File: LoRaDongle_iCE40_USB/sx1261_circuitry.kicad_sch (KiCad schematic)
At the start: 41 parts, among them J5 142-0701-801, J8 Jumper, U3 SX1261IMLTRT, U4 SKY13587-378LF, Y2 Crystal_GND24

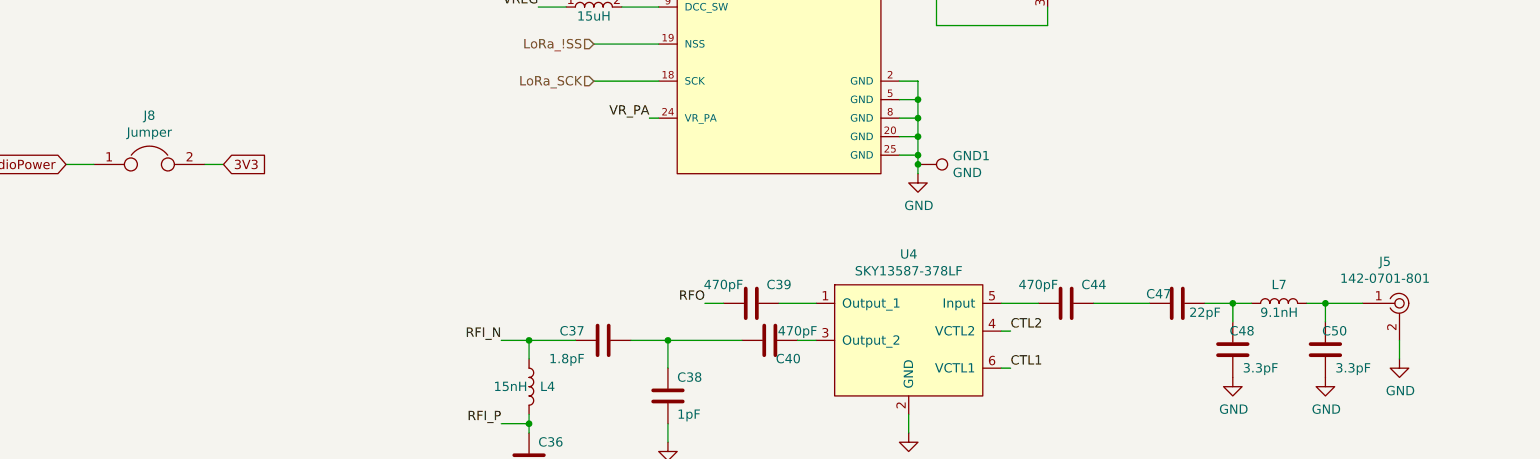
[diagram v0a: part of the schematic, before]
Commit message: added copper pours
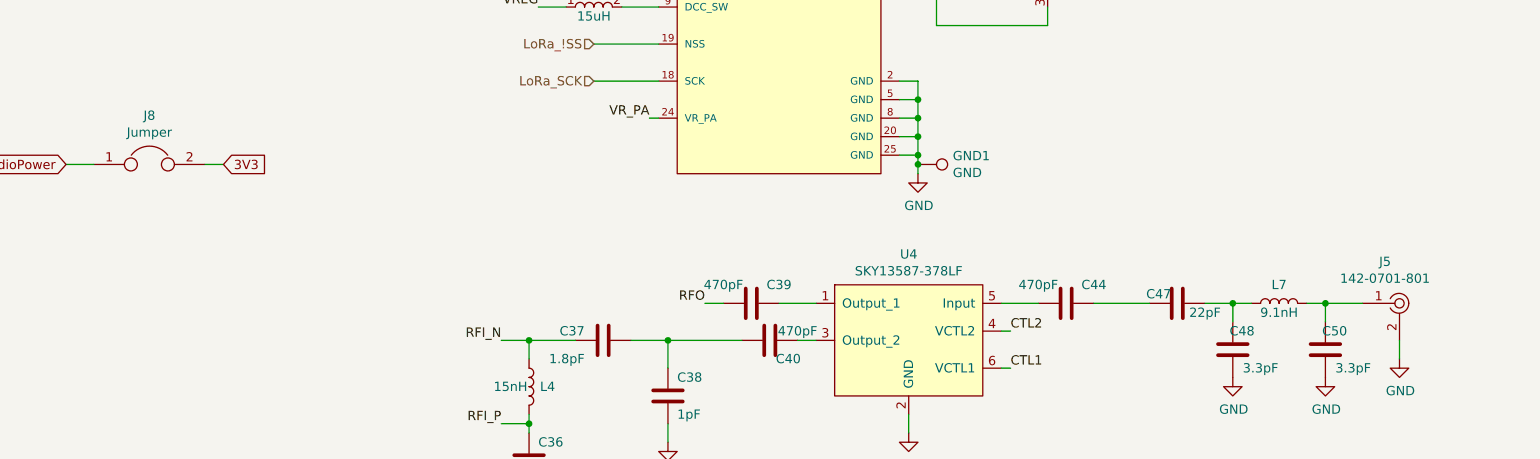
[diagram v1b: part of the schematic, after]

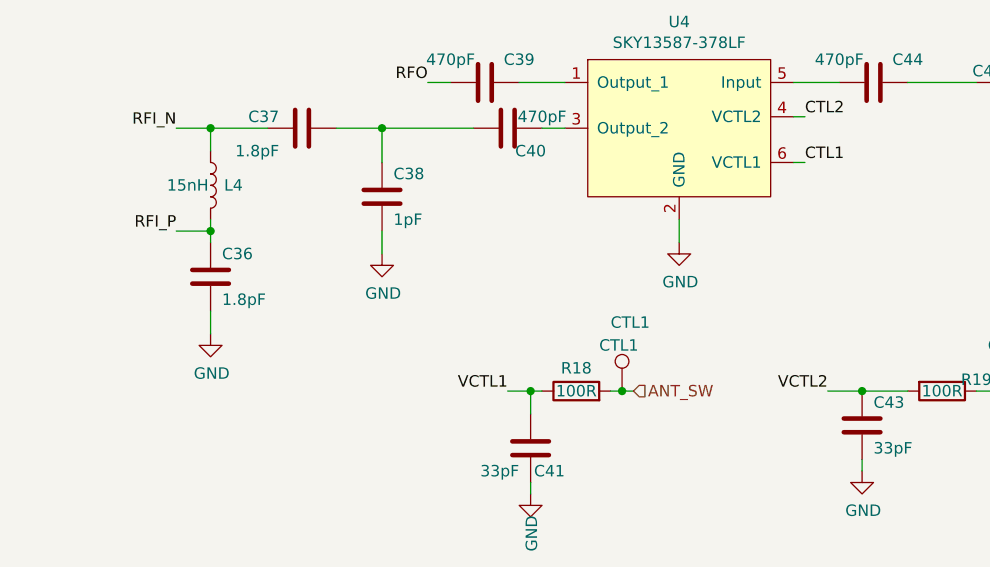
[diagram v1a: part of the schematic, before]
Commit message: updating symbol details
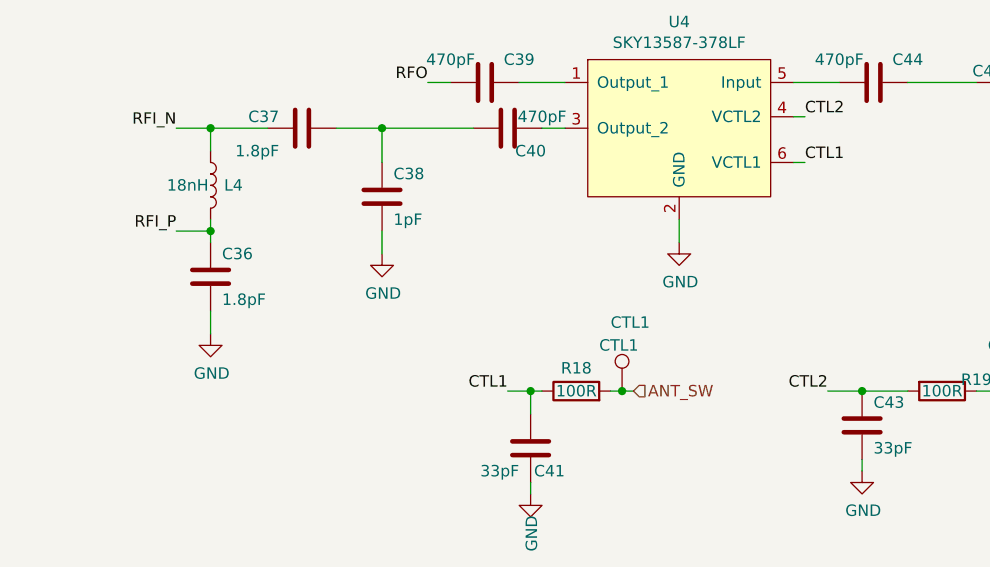
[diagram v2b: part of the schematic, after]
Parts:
- C33: Manufacturer (none) -> Murata Electronics; Manufacturer Part Number (none) -> GRM155R71C104KA88D; Package (none) -> 0402; Type (none) -> SMD
- C34: Manufacturer (none) -> Murata Electronics; Manufacturer Part Number (none) -> GRM155R70J105MA12D; Package (none) -> 0402; Part Number (none) -> GRM155R70J105MA12D; Type (none) -> SMD; part Number GRM188R61A105KA61D -> (none)
- C35: Manufacturer (none) -> Murata Electronics; Manufacturer Part Number (none) -> GRM155R71H103KA88J; Package (none) -> 0402; Part Number GRM1555C1H220JA01D -> GRM155R71H103KA88J; Type (none) -> SMD
- C36, C37: Manufacturer (none) -> Murata Electronics; Manufacturer Part Number (none) -> GRM1555C1H1R8WA01D; Package (none) -> 0402; Type (none) -> SMD; part Number GRM1555C1H1R8BA01D -> GRM1555C1H1R8WA01D
- C38: Manufacturer (none) -> Murata Electronics; Manufacturer Part Number (none) -> GRM1555C1H1R0BA01D; Package (none) -> 0402; Type (none) -> SMD
- C39, C40, C44: Manufacturer (none) -> Murata Electronics; Manufacturer Part Number (none) -> GRM1555C1H471JA01D; Package (none) -> 0402; Type (none) -> SMD
- C41, C43: Manufacturer (none) -> TDK Corporation; Manufacturer Part Number (none) -> CGA2B2C0G1H330J050BA; Package (none) -> 0402; Type (none) -> SMD
- C42: Manufacturer (none) -> Murata Electronics; Manufacturer Part Number (none) -> GRM155R61A474KE15D; Package (none) -> 0402; Type (none) -> SMD
- C45: Manufacturer (none) -> Murata Electronics; Manufacturer Part Number (none) -> GRM155R71C473KA01J; Package (none) -> 0402; Type (none) -> SMD
- C46: Manufacturer (none) -> Murata Electronics; Manufacturer Part Number (none) -> GRM1555C1H470JA01D; Package (none) -> 0402; Type (none) -> SMD
- C47: Manufacturer (none) -> Murata Electronics; Manufacturer Part Number (none) -> GRM1555C1H220FA01D; Package (none) -> 0402; Type (none) -> SMD
- C48, C50: Manufacturer (none) -> Murata Electronics; Manufacturer Part Number (none) -> GJM1555C1H3R3DB01D; Package (none) -> 0402; Type (none) -> SMD
- C49: Manufacturer (none) -> Murata Electronics; Manufacturer Part Number (none) -> GRM1555C1H3R0BA01J; Package (none) -> 0402; Part Number GRM1555C1H3R0BA01D -> GRM1555C1H3R0BA01J; Type (none) -> SMD
- C51: Manufacturer (none) -> Murata Electronics; Manufacturer Part Number (none) -> GRM1555C1H6R8BA01D; Package (none) -> 0402; Type (none) -> SMD
- C52: Manufacturer (none) -> Murata Electronics; Manufacturer Part Number (none) -> GRM1555C1H120JA01J; Package (none) -> 0402; Type (none) -> SMD
- CTL1, CTL2, GND1: Manufacturer (none) -> -; Manufacturer Part Number (none) -> -; Package (none) -> -; Type (none) -> -
- J5: Manufacturer Part Number (none) -> 142-0701-801; Package (none) -> Edge Connector; Type (none) -> SMD
- J8: Manufacturer (none) -> -; Manufacturer Part Number (none) -> -; Package (none) -> -; Type (none) -> Through Hole
- L3: Manufacturer (none) -> Murata Electronics; Manufacturer Part Number (none) -> LQW15AN47NJ00D; Package (none) -> 0402; Part Number (none) -> LQW15AN47NJ00D; Type (none) -> SMD
- L4: value 15nH -> 18nH; Manufacturer (none) -> Murata Electronics; Manufacturer Part Number (none) -> LQW15AN18NH00D; Package (none) -> 0402; Type (none) -> SMD
- L5: Manufacturer (none) -> TDK; Manufacturer Part Number (none) -> VLS201610CX-150M-1; Package (none) -> 2016; Type (none) -> SMD
- L6: Manufacturer (none) -> Murata Electronics; Manufacturer Part Number (none) -> LQW15AN47NJ00D; Package (none) -> 0402; PartNumber (none) -> LQW15AN47NJ00D; Type (none) -> SMD
- L7, L9: Manufacturer (none) -> Murata Electronics; Manufacturer Part Number (none) -> LQW15AN9N1H00D; Package (none) -> 0402; Type (none) -> SMD
- L8: Manufacturer (none) -> Murata Electronics; Manufacturer Part Number (none) -> LQW15AN2N7C00D
- R18, R19: Part Number CRCW0402100RFKED -> (none)
- U3: Manufacturer (none) -> Semtech; Manufacturer Part Number (none) -> SX1261IMLTRT; Package (none) -> QFN24; Type (none) -> SMD
- U4: Manufacturer (none) -> Skyworks Solutions Inc.; Manufacturer Part Number (none) -> SKY13587-378LF; Package (none) -> 6-MLPD; Type (none) -> SMD
- Y2: Manufacturer (none) -> ECS Inc.; Manufacturer Part Number (none) -> ECS-320-10-36B-CKM-TR; Package (none) -> 4 Pin Crystal; Type (none) -> SMD
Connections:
- net VCTL1 is gone; now on net CTL1: C41.2, R18.1
- net VCTL2 is gone; now on net CTL2: C43.1, R19.2

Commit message: updated BOM
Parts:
- D3, D4: Manufacturer (none) -> SunLED; Manufacturer Part Number (none) -> XZVG53W-8; Package (none) -> 0603
- R18, R19: Manufacturer (none) -> Stackpole Electronics Inc; Manufacturer Part Number (none) -> RMCF0402FT100R; Package (none) -> 0402
- R20, R21: value R -> 100R; Manufacturer (none) -> Stackpole Electronics Inc; Manufacturer Part Number (none) -> RMCF0402FT100R; Package (none) -> 0402
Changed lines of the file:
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@@
+      (effects (font (size 1.27 1.27)) hide)
+    )
+    (property "Description" "RES 100 OHM 1% 1/16W 0402" (id 5) (at 130.81 146.05 0)
+      (effects (font (size 1.27 1.27)) hide)
+    )
+    (property "Manufacturer" "Stackpole Electronics Inc" (id 6) (at 130.81 146.05 0)
+      (effects (font (size 1.27 1.27)) hide)
+    )
+    (property "Manufacturer Part Number" "RMCF0402FT100R" (id 7) (at 130.81 146.05 0)
+      (effects (font (size 1.27 1.27)) hide)
+    )
+    (property "Package" "0402" (id 8) (at 130.81 146.05 0)
       (effects (font (size 1.27 1.27)) hide)
     )
@@
       (effects (font (size 1.27 1.27)) (justify left))
     )
-    (property "Value" "R" (id 1) (at 249.428 128.143 0)
+    (property "Value" "100R" (id 1) (at 249.428 128.143 0)
       (effects (font (size 1.27 1.27)) (justify left))
     )
@@
     )
     (property "Datasheet" "~" (id 3) (at 247.65 127 0)
+      (effects (font (size 1.27 1.27)) hide)
+    )
+    (property "Description" "RES 100 OHM 1% 1/16W 0402" (id 4) (at 247.65 127 0)
+      (effects (font (size 1.27 1.27)) hide)
+    )
+    (property "Manufacturer" "Stackpole Electronics Inc" (id 5) (at 247.65 127 0)
+      (effects (font (size 1.27 1.27)) hide)
+    )
+    (property "Manufacturer Part Number" "RMCF0402FT100R" (id 6) (at 247.65 127 0)
+      (effects (font (size 1.27 1.27)) hide)
+    )
+    (property "Package" "0402" (id 7) (at 247.65 127 0)
       (effects (font (size 1.27 1.27)) hide)
     )
@@
       (effects (font (size 1.27 1.27)) hide)
     )
+    (property "Description" "LED GREEN CLEAR CHIP SMD" (id 4) (at 247.65 135.89 0)
+      (effects (font (size 1.27 1.27)) hide)
+    )
+    (property "Manufacturer" "SunLED" (id 5) (at 247.65 135.89 0)
+      (effects (font (size 1.27 1.27)) hide)
+    )
+    (property "Manufacturer Part Number" "XZVG53W-8" (id 6) (at 247.65 135.89 0)
+      (effects (font (size 1.27 1.27)) hide)
+    )
+    (property "Package" "0603" (id 7) (at 247.65 135.89 0)
+      (effects (font (size 1.27 1.27)) hide)
+    )
     (pin "1")
     (pin "2")
@@
       (effects (font (size 1.27 1.27)) (justify left))
     )
-    (property "Value" "R" (id 1) (at 263.398 128.143 0)
+    (property "Value" "100R" (id 1) (at 263.398 128.143 0)
       (effects (font (size 1.27 1.27)) (justify left))
     )
@@
     )
     (property "Datasheet" "~" (id 3) (at 261.62 127 0)
+      (effects (font (size 1.27 1.27)) hide)
+    )
+    (property "Description" "RES 100 OHM 1% 1/16W 0402" (id 4) (at 261.62 127 0)
+      (effects (font (size 1.27 1.27)) hide)
+    )
+    (property "Manufacturer" "Stackpole Electronics Inc" (id 5) (at 261.62 127 0)
+      (effects (font (size 1.27 1.27)) hide)
+    )
+    (property "Manufacturer Part Number" "RMCF0402FT100R" (id 6) (at 261.62 127 0)
+      (effects (font (size 1.27 1.27)) hide)
+    )
+    (property "Package" "0402" (id 7) (at 261.62 127 0)
       (effects (font (size 1.27 1.27)) hide)
     )
@@
     )
     (property "Datasheet" "~" (id 3) (at 261.62 135.89 0)
+      (effects (font (size 1.27 1.27)) hide)
+    )
+    (property "Description" "LED GREEN CLEAR CHIP SMD" (id 4) (at 261.62 135.89 0)
+      (effects (font (size 1.27 1.27)) hide)
+    )
+    (property "Manufacturer" "SunLED" (id 5) (at 261.62 135.89 0)
+      (effects (font (size 1.27 1.27)) hide)
+    )
+    (property "Manufacturer Part Number" "XZVG53W-8" (id 6) (at 261.62 135.89 0)
+      (effects (font (size 1.27 1.27)) hide)
+    )
+    (property "Package" "0603" (id 7) (at 261.62 135.89 0)
       (effects (font (size 1.27 1.27)) hide)
     )
@@
       (effects (font (size 1.27 1.27)) hide)
     )
+    (property "Description" "RES 100 OHM 1% 1/16W 0402" (id 5) (at 171.45 146.05 0)
+      (effects (font (size 1.27 1.27)) hide)
+    )
+    (property "Manufacturer" "Stackpole Electronics Inc" (id 6) (at 171.45 146.05 0)
+      (effects (font (size 1.27 1.27)) hide)
+    )
+    (property "Manufacturer Part Number" "RMCF0402FT100R" (id 7) (at 171.45 146.05 0)
+      (effects (font (size 1.27 1.27)) hide)
+    )
+    (property "Package" "0402" (id 8) (at 171.45 146.05 0)
+      (effects (font (size 1.27 1.27)) hide)
+    )

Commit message: updating silkscreen
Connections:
- net DIO3: no longer names the net of U3.6 (DIO3)
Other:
- note removed: "To be completed"
- title: LoRa Dongle -> RiscVLoRaDongle
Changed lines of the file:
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@@
   (paper "A4")
   (title_block
-    (title "LoRa Dongle")
+    (title "RiscVLoRaDongle")
+    (date "2022-02-03")
+    (rev "1.0")
     (company "Mark Njoroge")
   )
@@
   (junction (at 162.56 146.05) (diameter 0) (color 0 0 0 0)
   )
+  (junction (at 104.14 86.36) (diameter 0) (color 0 0 0 0)
+  )
   (junction (at 90.17 116.84) (diameter 0) (color 0 0 0 0)
   )
@@
   )
   (no_connect (at 104.14 45.72))
+  (wire (pts (xy 104.14 45.72) (xy 107.95 45.72))
+    (stroke (width 0) (type default) (color 0 0 0 0))
+  )
   (wire (pts (xy 143.51 88.9) (xy 143.51 91.44))
     (stroke (width 0) (type default) (color 0 0 0 0))
@@
     (stroke (width 0) (type default) (color 0 0 0 0))
   )
+  (wire (pts (xy 104.14 86.36) (xy 107.95 86.36))
+    (stroke (width 0) (type default) (color 0 0 0 0))
+  )
   (wire (pts (xy 166.37 67.31) (xy 167.64 67.31))
     (stroke (width 0) (type default) (color 0 0 0 0))
@@
     (stroke (width 0) (type default) (color 0 0 0 0))
   )
-  (wire (pts (xy 107.95 45.72) (xy 104.14 45.72))
-    (stroke (width 0) (type default) (color 0 0 0 0))
-  )
   (wire (pts (xy 125.73 148.59) (xy 125.73 146.05))
     (stroke (width 0) (type default) (color 0 0 0 0))
@@
     (stroke (width 0) (type default) (color 0 0 0 0))
   )
-  (wire (pts (xy 106.68 86.36) (xy 107.95 86.36))
+  (wire (pts (xy 101.6 86.36) (xy 104.14 86.36))
     (stroke (width 0) (type default) (color 0 0 0 0))
   )
@@
   (wire (pts (xy 156.21 67.31) (xy 154.94 67.31))
     (stroke (width 0) (type default) (color 0 0 0 0))
-  )
-  (text "To be completed" (at 247.65 151.13 0)
-    (effects (font (size 1.27 1.27)) (justify left bottom))
   )
   (text "VBAT decoupling Caps" (at 34.29 58.42 0)
@@
     (effects (font (size 1.27 1.27)) (justify right bottom))
   )
-  (label "VBAT" (at 45.72 38.1 0)
-    (effects (font (size 1.27 1.27)) (justify left bottom))
-  )
   (label "RFI_P" (at 86.36 128.27 180)
     (effects (font (size 1.27 1.27)) (justify right bottom))
@@
     (effects (font (size 1.27 1.27)) (justify right bottom))
   )
-  (label "DIO3" (at 104.14 45.72 180)
-    (effects (font (size 1.27 1.27)) (justify right bottom))
-  )
-  (label "VBAT" (at 104.14 52.07 180)
-    (effects (font (size 1.27 1.27)) (justify right bottom))
-  )
   (label "CTL1" (at 123.19 146.05 180)
     (effects (font (size 1.27 1.27)) (justify right bottom))
   )
-  (label "VR_PA" (at 106.68 86.36 180)
+  (label "VR_PA" (at 101.6 86.36 180)
     (effects (font (size 1.27 1.27)) (justify right bottom))
   )
@@
       (effects (font (size 1.27 1.27)) hide)
     )
+    (pin "1")
+  )
+  (symbol (lib_id "power:PWR_FLAG") (at 104.14 86.36 180) (unit 1)
+    (in_bom yes) (on_board yes) (fields_autoplaced)
+    (property "Reference" "#FLG04" (id 0) (at 104.14 88.265 0)
+      (effects (font (size 1.27 1.27)) hide)
+    )
+    (property "Value" "PWR_FLAG" (id 1) (at 104.14 91.44 0))
+    (property "Footprint" "" (id 2) (at 104.14 86.36 0)
+      (effects (font (size 1.27 1.27)) hide)
+    )
+    (property "Datasheet" "~" (id 3) (at 104.14 86.36 0)
+      (effects (font (size 1.27 1.27)) hide)
+    )
